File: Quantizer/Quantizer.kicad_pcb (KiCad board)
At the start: 2 copper layers, 100 x 200 mm, 4 parts, among them J1 EuroPower

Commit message: Quantizer layout done!
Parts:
- removed H3: Panel, Kosmo_panel:Kosmo_Panel_Dual_Mounting_Holes
- added C1: 10u, Capacitor_THT:CP_Radial_D4.0mm_P1.50mm, B.Cu at (33.7, 29.8)
- added C2: 1u, Capacitor_THT:CP_Radial_D4.0mm_P1.50mm, B.Cu at (15.4, 41.4)
- added C3: 100n, Capacitor_SMD:C_1206_3216Metric_Pad1.42x1.75mm_HandSolder, B.Cu at (16.6, 48.9)
- added C4: 100n, Capacitor_SMD:C_1206_3216Metric_Pad1.42x1.75mm_HandSolder, F.Cu at (20.5, 84.1)
- added C5: 100n, Capacitor_SMD:C_1206_3216Metric_Pad1.42x1.75mm_HandSolder, F.Cu at (31.5, 84.0)
- added C6: 100n, Capacitor_SMD:C_1206_3216Metric_Pad1.42x1.75mm_HandSolder, B.Cu at (13.4, 155.0)
- added C7: 100n, Capacitor_SMD:C_1206_3216Metric_Pad1.42x1.75mm_HandSolder, B.Cu at (14.0, 160.1)
- added D1: 1N4148, Diode_SMD:D_1206_3216Metric_Pad1.42x1.75mm_HandSolder, B.Cu at (24.0, 167.0)
- added D2: 1N4148, Diode_SMD:D_1206_3216Metric_Pad1.42x1.75mm_HandSolder, B.Cu at (21.7, 167.0)
- added D3: 1N4148, Diode_SMD:D_1206_3216Metric_Pad1.42x1.75mm_HandSolder, B.Cu at (24.0, 127.0)
- added D4: 1N4148, Diode_SMD:D_1206_3216Metric_Pad1.42x1.75mm_HandSolder, B.Cu at (21.7, 127.0)
- added D5: 1N4148, Diode_SMD:D_1206_3216Metric_Pad1.42x1.75mm_HandSolder, B.Cu at (24.0, 86.4)
- added D6: 1N4148, Diode_SMD:D_1206_3216Metric_Pad1.42x1.75mm_HandSolder, B.Cu at (21.7, 86.4)
- added J2: Prog, TestPoint:TestPoint_Pad_D2.5mm, B.Cu at (17.6, 56.9)
- added J3: IN1, telec:JackHole, F.Cu at (27.1, 176.2)
- added J4: IN2, telec:JackHole, F.Cu at (27.1, 136.2)
- added J5: IN3, telec:JackHole, F.Cu at (27.1, 96.2)
- added J6: OUT1, telec:JackHole, F.Cu at (22.1, 196.2)
- added J7: OUT2, telec:JackHole, F.Cu at (22.1, 156.2)
- added J8: OUT3, telec:JackHole, F.Cu at (22.1, 116.2)
- added LOGO1: telec, logo:telec-8, F.Cu at (24.6, 16.3)
- added R1: 100k, Resistor_SMD:R_1206_3216Metric_Pad1.42x1.75mm_HandSolder, B.Cu at (19.4, 167.0)
- added R2: 100k, Resistor_SMD:R_1206_3216Metric_Pad1.42x1.75mm_HandSolder, B.Cu at (19.4, 127.0)
- added R3: 100k, Resistor_SMD:R_1206_3216Metric_Pad1.42x1.75mm_HandSolder, B.Cu at (19.4, 86.4)
- added R4: 1k, Resistor_SMD:R_1206_3216Metric_Pad1.42x1.75mm_HandSolder, B.Cu at (13.3, 174.5)
- added R5: 1k, Resistor_SMD:R_1206_3216Metric_Pad1.42x1.75mm_HandSolder, B.Cu at (13.3, 134.4)
- added R6: 1k, Resistor_SMD:R_1206_3216Metric_Pad1.42x1.75mm_HandSolder, B.Cu at (13.3, 94.3)
- added RV1: 100k, Potentiometer_THT:Potentiometer_Alps_RK09K_Single_Vertical, F.Cu at (27.1, 67.9)
- added RV2: 100k, Potentiometer_THT:Potentiometer_Alps_RK09K_Single_Vertical, F.Cu at (22.1, 29.6)
- added U1: L7805, Package_TO_SOT_THT:TO-220-3_Vertical, B.Cu at (16.0, 31.1)
- added U2: TL082, Package_SO:SOIC-8_3.9x4.9mm_P1.27mm, B.Cu at (15.0, 166.9)
- added U3: TL082, Package_SO:SOIC-8_3.9x4.9mm_P1.27mm, B.Cu at (15.0, 126.9)
- added U4: TL082, Package_SO:SOIC-8_3.9x4.9mm_P1.27mm, B.Cu at (15.0, 86.9)
- added U5: ATtiny416-S, Package_SO:SOIC-20W_7.5x12.8mm_P1.27mm, B.Cu at (24.6, 48.8)
- added U6: MCP4801, Package_DIP:DIP-8_W7.62mm, F.Cu at (35.3, 74.0)
- added U7: MCP4801, Package_DIP:DIP-8_W7.62mm, F.Cu at (24.3, 74.0)
- H1, H2: value Panel -> Mounting_Holes
- moved H2 28.6 mm to (34.1, 209.1)
- moved J1 7.96 mm to (29.7, 24.4)
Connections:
- J1 pad 1: (no net) -> -12V
- J1 pad 2: (no net) -> GND
- J1 pad 3: (no net) -> +12V
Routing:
- net +5V: track 0.00 -> 232.0 mm, vias 0 -> 4
- net +12V: track 0.00 -> 177.8 mm, vias 0 -> 4
- net -12V: track 0.00 -> 165.5 mm, vias 0 -> 3
- net /IN1: track 0.00 -> 155.0 mm, vias 0 -> 4
- net /IN2: track 0.00 -> 115.7 mm, vias 0 -> 2
- net Net-(U2-Pad5): track 0.00 -> 105.7 mm
- net Net-(U3-Pad5): track 0.00 -> 71.6 mm
- net Net-(J8-PadT): track 0.00 -> 66.2 mm
- net Net-(J7-PadT): track 0.00 -> 66.2 mm
- net Net-(J6-PadT): track 0.00 -> 66.2 mm
- net /DAC0: track 0.00 -> 55.8 mm
- net /IN3: track 0.00 -> 53.8 mm
- net /SCK: track 0.00 -> 48.3 mm
- net /~LDAC: track 0.00 -> 45.7 mm
- net /MOSI: track 0.00 -> 40.8 mm
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- added copper zone on B.Cu, net GND
- added copper zone on F.Cu, net GND
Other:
- board size 100 x 200 mm -> 25 x 200 mm
- board text added: "Triple Quantizer"

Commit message: Quantizer done!
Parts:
- added C8: 100n, Capacitor_SMD:C_1206_3216Metric_Pad1.42x1.75mm_HandSolder, F.Cu at (33.8, 84.1)
- added C9: 100n, Capacitor_SMD:C_1206_3216Metric_Pad1.42x1.75mm_HandSolder, F.Cu at (22.8, 84.1)
- added SW1: Bank, Connector_PinHeader_2.54mm:PinHeader_1x03_P2.54mm_Vertical, F.Cu at (35.6, 51.4)
- moved C4 13.3 mm to (24.9, 71.5)
- moved C5 12.6 mm to (33.1, 71.5), turned to 0 degrees
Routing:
- net Net-(SW1-Pad2): track 0.00 -> 9.44 mm
- net /~LDAC: track 45.7 -> 48.9 mm, vias 0 -> 1
- net Net-(C8-Pad2): track 105.7 -> 108.3 mm
- net Net-(C9-Pad2): track 71.6 -> 74.0 mm
- net +5V: track 232.0 -> 233.8 mm
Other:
- board text added: "1"
- board text added: "2"
- board text added: "3"
- board text added: "4"
- board text added: "5"
- board text added: "6"
- board text added: "7"
- board text added: "8"
- board text added: "A"
- board text added: "B"
- board text added: "Design by telec"
- board text added: "PCB ref here:"
- board text added: "UPDI"

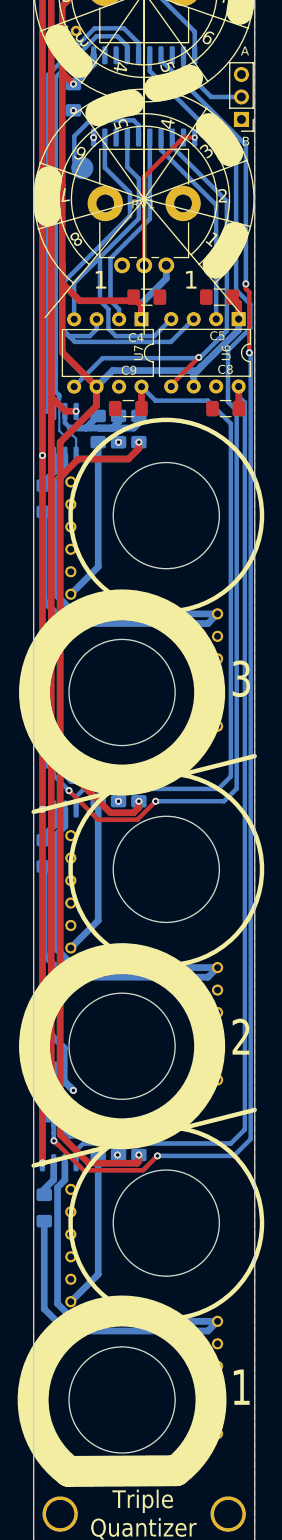
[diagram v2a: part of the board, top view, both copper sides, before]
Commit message: updated footprints on Quantizer
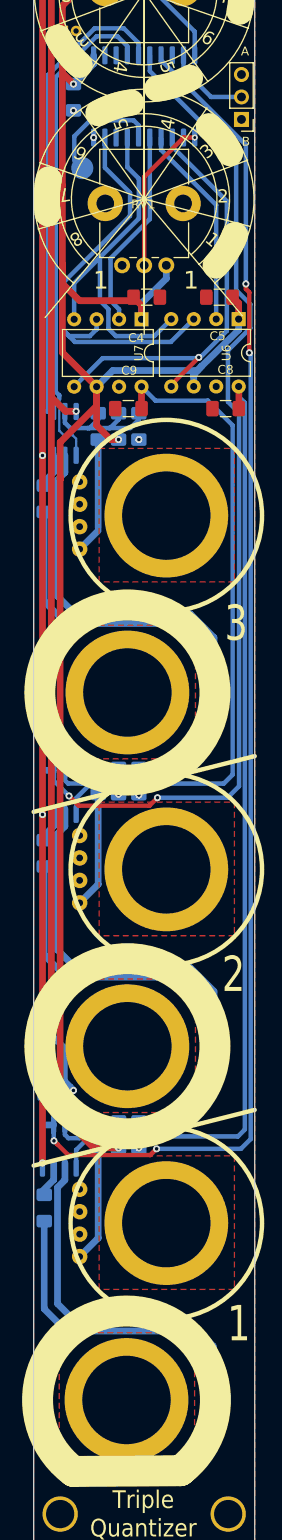
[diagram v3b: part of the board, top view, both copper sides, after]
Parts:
- J3, J4, J5, J6, J7, J8: footprint telec:JackHole -> telec:Jack_Hole_Square
- moved D1 2.44 mm to (21.7, 166.2)
- moved D2 2.44 mm to (24.0, 166.2)
- moved D3 2.44 mm to (21.7, 126.2)
- moved D4 2.43 mm to (24.0, 126.2)
- moved D5 2.32 mm to (21.7, 86.1)
- moved D6 2.32 mm to (24.0, 86.1)
- moved R1 0.80 mm to (19.4, 166.2)
- moved R2 0.80 mm to (19.4, 126.2)
- moved C7 0.60 mm to (13.4, 160.2)
- moved J7 0.60 mm to (22.7, 156.2)
- moved J8 0.60 mm to (22.7, 116.2)
- moved U2 0.60 mm to (15.0, 167.5)
- moved U3 0.60 mm to (15.0, 127.5)
- moved J6 0.50 mm to (22.6, 196.2)
- moved R3 0.30 mm to (19.4, 86.1)
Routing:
- net +5V: track 233.8 -> 219.4 mm
- net Net-(J5-PadT): track 18.5 -> 13.0 mm
- net Net-(J3-PadT): track 18.0 -> 13.2 mm
- net Net-(J4-PadT): track 17.9 -> 13.2 mm
- net Net-(J7-PadT): track 66.2 -> 70.1 mm
- net Net-(J8-PadT): track 66.2 -> 70.1 mm
- net Net-(J6-PadT): track 66.2 -> 69.9 mm
- net Net-(D3-Pad2): track 13.2 -> 10.8 mm
- net Net-(D1-Pad2): track 13.6 -> 11.6 mm
- net /IN1: track 155.0 -> 153.7 mm
- net Net-(C9-Pad2): track 74.0 -> 74.7 mm
- net -12V: track 165.5 -> 166.2 mm
- net Net-(C8-Pad2): track 108.3 -> 108.9 mm
- net Net-(D5-Pad2): track 16.2 -> 15.5 mm
